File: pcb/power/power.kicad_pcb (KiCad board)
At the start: 2 copper layers, 50 x 40 mm, 233 parts, among them CON1 BARREL_JACK, P1 CONN_01X04, P2 CONN_01X04, P3 CONN_01X04, P4 USB_A, P5 CONN_01X03, P6 CONN_01X03, Q1 MMBT3904, Q2 MMBT3904, Q3 MMBT3904, Q4 MMBT3904, Q5 MMBT3904, Q6 MMBT3904, Q7 DMG2305UX, Q8 DMG2305UX, Q9 DMG2305UX, U1 LM2840, U2 TS30012, U3 TPS2514ADBV, U4 LM324QT

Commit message: Fixed the board. This is rev 2.
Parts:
- removed the REF** at (175.9, 120.0)
- removed the REF** at (160.5, 104.5)
- removed the REF** at (158.0, 101.1)
- removed the REF** at (158.0, 89.3)
- removed the REF** at (149.1, 109.5)
- removed the REF** at (138.0, 113.6)
- removed the REF** at (138.0, 110.3)
- removed the REF** at (166.2, 95.4)
- removed the REF** at (138.0, 111.9)
- removed the REF** at (137.7, 116.7)
- removed the REF** at (145.9, 114.7)
- removed the REF** at (134.6, 98.0)
- removed the REF** at (134.6, 99.3)
- removed the REF** at (134.6, 100.6)
- removed the REF** at (166.9, 90.9)
- removed the REF** at (143.9, 113.9)
- removed the REF** at (165.6, 89.3)
- removed the REF** at (162.1, 86.7)
- removed the REF** at (160.5, 89.3)
- removed the REF** at (159.3, 89.3)
- removed the REF** at (149.9, 95.1)
- added REF**: Via_GND_04, Additional:Via_GND_04, F.Cu at (178.4, 107.2)
- added REF**: Via_GND_04, Additional:Via_GND_04, F.Cu at (173.0, 121.2)
- added REF**: Via_GND_04, Additional:Via_GND_04, F.Cu at (165.1, 108.5)
- added REF**: Via_GND_04, Additional:Via_GND_04, F.Cu at (162.4, 115.7)
- added REF**: Via_GND_04, Additional:Via_GND_04, F.Cu at (158.0, 89.7)
- added REF**: Via_GND_04, Additional:Via_GND_04, F.Cu at (162.3, 110.0)
- added REF**: Via_GND_04, Additional:Via_GND_04, F.Cu at (177.5, 111.8)
- added REF**: Via_GND_04, Additional:Via_GND_04, F.Cu at (141.7, 101.9)
- added REF**: Via_GND_04, Additional:Via_GND_04, F.Cu at (158.0, 100.6)
- added REF**: Via_GND_04, Additional:Via_GND_04, F.Cu at (164.8, 112.5)
- added REF**: Via_GND_04, Additional:Via_GND_04, F.Cu at (160.0, 89.7)
- added REF**: Via_GND_04, Additional:Via_GND_04, F.Cu at (137.4, 93.7)
- added REF**: Via_GND_04, Additional:Via_GND_04, F.Cu at (146.1, 114.8)
- added REF**: Via_GND_04, Additional:Via_GND_04, F.Cu at (147.1, 93.0)
- added REF**: Via_GND_04, Additional:Via_GND_04, F.Cu at (170.9, 121.2)
- added REF**: Via_GND_04, Additional:Via_GND_04, F.Cu at (131.8, 93.7)
- added REF**: Via_GND_04, Additional:Via_GND_04, F.Cu at (144.0, 113.8)
- added REF**: Via_GND_04, Additional:Via_GND_04, F.Cu at (158.0, 102.1)
- added REF**: Via_GND_04, Additional:Via_GND_04, F.Cu at (167.1, 90.7)
- added REF**: Via_GND_04, Additional:Via_GND_04, F.Cu at (154.4, 99.6)
- added REF**: Via_GND_04, Additional:Via_GND_04, F.Cu at (173.7, 111.8)
- added REF**: Via_GND_04, Additional:Via_GND_04, F.Cu at (137.7, 114.0)
- added REF**: Via_GND_04, Additional:Via_GND_04, F.Cu at (158.0, 121.4)
- added REF**: Via_GND_04, Additional:Via_GND_04, F.Cu at (152.0, 99.9)
- added REF**: Via_GND_04, Additional:Via_GND_04, F.Cu at (176.3, 121.2)
- added REF**: Via_GND_04, Additional:Via_GND_04, F.Cu at (148.0, 119.1)
- added REF**: Via_GND_04, Additional:Via_GND_04, F.Cu at (175.0, 111.8)
- added REF**: Via_GND_04, Additional:Via_GND_04, F.Cu at (171.7, 118.1)
- added REF**: Via_GND_04, Additional:Via_GND_04, F.Cu at (175.0, 115.8)
- added REF**: Via_GND_04, Additional:Via_GND_04, F.Cu at (162.6, 95.2)
- added REF**: Via_GND_04, Additional:Via_GND_04, F.Cu at (148.2, 97.9)
- added REF**: Via_GND_04, Additional:Via_GND_04, F.Cu at (137.7, 107.2)
- added REF**: Via_GND_04, Additional:Via_GND_04, F.Cu at (137.7, 105.4)
- added REF**: Via_GND_04, Additional:Via_GND_04, F.Cu at (145.5, 114.0)
- added REF**: Via_GND_04, Additional:Via_GND_04, F.Cu at (155.7, 118.4)
- added REF**: Via_GND_04, Additional:Via_GND_04, F.Cu at (146.8, 109.5)
- added REF**: Via_GND_04, Additional:Via_GND_04, F.Cu at (165.9, 90.7)
- added REF**: Via_GND_04, Additional:Via_GND_04, F.Cu at (134.9, 110.2)
- added REF**: Via_GND_04, Additional:Via_GND_04, F.Cu at (173.5, 118.1)
- added REF**: Via_GND_04, Additional:Via_GND_04, F.Cu at (149.4, 109.5)
- added REF**: Via_GND_04, Additional:Via_GND_04, F.Cu at (134.9, 97.0)
- added REF**: Via_GND_04, Additional:Via_GND_04, F.Cu at (140.7, 97.0)
- added REF**: Via_GND_04, Additional:Via_GND_04, F.Cu at (131.8, 92.5)
- added REF**: Via_GND_04, Additional:Via_GND_04, F.Cu at (161.5, 100.3)
- added REF**: Via_GND_04, Additional:Via_GND_04, F.Cu at (137.4, 92.5)
- added REF**: Via_GND_04, Additional:Via_GND_04, F.Cu at (137.7, 111.5)
- added REF**: Via_GND_04, Additional:Via_GND_04, F.Cu at (178.4, 108.3)
- added REF**: Via_GND_04, Additional:Via_GND_04, F.Cu at (166.4, 104.9)
- added REF**: Via_GND_04, Additional:Via_GND_04, F.Cu at (149.5, 118.4)
- added REF**: Via_GND_04, Additional:Via_GND_04, F.Cu at (158.8, 115.1)
- added REF**: Via_GND_04, Additional:Via_GND_04, F.Cu at (160.0, 102.1)
- added REF**: Via_GND_04, Additional:Via_GND_04, F.Cu at (175.0, 113.8)
- added REF**: Via_GND_04, Additional:Via_GND_04, F.Cu at (161.0, 121.4)
- added REF**: Via_GND_04, Additional:Via_GND_04, F.Cu at (158.0, 122.7)
- added REF**: Via_GND_04, Additional:Via_GND_04, F.Cu at (175.0, 118.1)
- added REF**: Via_GND_04, Additional:Via_GND_04, F.Cu at (145.5, 90.2)
- added REF**: Via_GND_04, Additional:Via_GND_04, F.Cu at (137.7, 112.8)
- added REF**: Via_GND_04, Additional:Via_GND_04, F.Cu at (166.4, 119.4)
- added REF**: Via_GND_04, Additional:Via_GND_04, F.Cu at (142.2, 97.0)
- added REF**: Via_GND_04, Additional:Via_GND_04, F.Cu at (138.9, 99.6)
- Q1, Q2, Q3, Q4, Q5, Q6, Q7, Q8, Q9: footprint TO_SOT_Packages_SMD:SOT-23_Handsoldering -> TO_SOT_Packages_SMD:SOT-23
- moved REF** 42.4 mm to (136.7, 97.0)
- moved REF** 42.2 mm to (136.7, 99.6)
- moved REF** 28.7 mm to (134.9, 98.3)
- moved REF** 28.7 mm to (153.7, 89.7)
- moved REF** 28.0 mm to (134.9, 99.6)
- moved REF** 27.5 mm to (137.7, 110.2)
- moved REF** 27.1 mm to (136.7, 100.8)
- moved REF** 27.1 mm to (155.2, 89.7)
- moved REF** 26.8 mm to (134.9, 100.8)
- moved REF** 25.0 mm to (136.7, 98.3)
- moved REF** 20.0 mm to (176.0, 107.2)
- moved REF** 18.4 mm to (158.8, 116.6)
- moved REF** 18.0 mm to (161.0, 105.2)
- moved REF** 14.9 mm to (178.3, 116.3)
- moved REF** 14.5 mm to (160.0, 104.1)
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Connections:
- C11 pad 1: PWM_OLED -> Net-(C11-Pad1)
- Q1 pad 2: Net-(D6-Pad1) -> LED_GND
- Q1 pad 3: LED_GND -> Net-(D6-Pad1)
- Q2 pad 2: Net-(D7-Pad1) -> LED_GND
- Q2 pad 3: LED_GND -> Net-(D7-Pad1)
- Q3 pad 2: Net-(D8-Pad1) -> LED_GND
- Q3 pad 3: LED_GND -> Net-(D8-Pad1)
- Q4 pad 2: V20 -> Net-(D6-Pad2)
- Q4 pad 3: Net-(D6-Pad2) -> V20
- Q5 pad 2: V20 -> Net-(D7-Pad2)
- Q5 pad 3: Net-(D7-Pad2) -> V20
- Q6 pad 2: V20 -> Net-(D8-Pad2)
- Q6 pad 3: Net-(D8-Pad2) -> V20
- Q7 pad 1: V20 -> Net-(D6-Pad2)
- Q7 pad 2: Net-(D6-Pad2) -> V20
- Q8 pad 1: V20 -> Net-(D7-Pad2)
- Q8 pad 2: Net-(D7-Pad2) -> V20
- Q9 pad 1: V20 -> Net-(D8-Pad2)
- Q9 pad 2: Net-(D8-Pad2) -> V20
- R18 pad 1: Net-(C9-Pad1) -> PWM_OLED
- R18 pad 2: Net-(R18-Pad2) -> Net-(C11-Pad1)
- R20 pad 1: PWM_OLED -> Net-(C11-Pad1)
- U4 pad 12: Net-(R18-Pad2) -> Net-(C9-Pad1)
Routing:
- net Net-(C12-Pad1): track 22.3 -> 3.37 mm
- net Net-(C4-Pad2): track 25.1 -> 17.2 mm
- net LED_R: track 83.2 -> 89.1 mm, vias 6 -> 5
- net V20: track 178.9 -> 174.4 mm
- net Net-(R18-Pad2): track 4.44 -> 0.00 mm
- net Net-(C11-Pad1): track 0.00 -> 4.42 mm, vias 0 -> 2
- net Net-(C9-Pad1): track 5.36 -> 9.69 mm
- net Net-(C13-Pad1): track 9.96 -> 5.96 mm
- net Net-(C2-Pad1): track 7.30 -> 3.54 mm
- net Net-(D8-Pad1): track 16.4 -> 13.3 mm
- net Net-(C4-Pad1): track 4.50 -> 1.54 mm
- net Net-(D7-Pad1): track 12.9 -> 10.0 mm
- net Net-(D6-Pad1): track 7.81 -> 10.6 mm, vias 2 -> 1
- net V28: track 28.7 -> 31.5 mm
- net PWM_OLED: track 51.8 -> 49.1 mm, vias 3 -> 1
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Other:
- net class Default: clearance 0.2 -> 0.19
- rule trace_clearance: 0.2 -> 0.19
- board text removed: "C22"
- board text removed: "D10"
- board text removed: "D11"
- board text removed: "D2"
- board text removed: "D4"
- board text removed: "D6"
- board text removed: "D7"
- board text removed: "D8"
- board text removed: "D9"
- board text removed: "U3"

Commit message: Some minor changes. Rev2 ready now.
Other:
- board text added: "Max & Elmar February 2017"
- board text added: "Swakeup Power Rev2"
- board text removed: "Max & Elmar December 2016"
- board text removed: "Swakeup Power Rev1"
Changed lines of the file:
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@@
   (layers
     (0 F.Cu signal)
-    (31 B.Cu signal)
+    (31 B.Cu signal hide)
     (32 B.Adhes user hide)
-    (33 F.Adhes user hide)
+    (33 F.Adhes user)
     (34 B.Paste user hide)
     (35 F.Paste user hide)
     (36 B.SilkS user hide)
-    (37 F.SilkS user)
+    (37 F.SilkS user hide)
     (38 B.Mask user hide)
     (39 F.Mask user hide)
@@
   )
   (setup
-    (last_trace_width 0.25)
+    (last_trace_width 0.75)
     (user_trace_width 0.5)
     (user_trace_width 0.75)
@@
     (tags SOT-23)
     (attr smd)
-    (fp_text reference Q9 (at -1.778 -1.651 360) (layer F.SilkS)
+    (fp_text reference Q9 (at 0 2.54 360) (layer F.SilkS)
       (effects (font (size 1 1) (thickness 0.15)))
     )
@@
     (tags SOT-23)
     (attr smd)
-    (fp_text reference Q7 (at -2.413 0 360) (layer F.SilkS)
+    (fp_text reference Q7 (at 0 2.667 360) (layer F.SilkS)
       (effects (font (size 1 1) (thickness 0.15)))
     )
@@
     (tags SOT-23)
     (attr smd)
-    (fp_text reference Q6 (at -1.397 -2.032 180) (layer F.SilkS)
+    (fp_text reference Q6 (at 0 2.667 180) (layer F.SilkS)
       (effects (font (size 1 1) (thickness 0.15)))
     )
@@
     (tags SOT-23)
     (attr smd)
-    (fp_text reference Q5 (at 0 2.54 360) (layer F.SilkS)
+    (fp_text reference Q5 (at 0 -2.54 360) (layer F.SilkS)
       (effects (font (size 1 1) (thickness 0.15)))
     )
@@
     (tags SOT-23)
     (attr smd)
-    (fp_text reference Q4 (at 0 -4.191 180) (layer F.SilkS)
+    (fp_text reference Q4 (at 0 2.54 180) (layer F.SilkS)
       (effects (font (size 1 1) (thickness 0.15)))
     )
@@
   (module Additional:Bourns_SRN3015 (layer F.Cu)
     (at 174.4726 102.616 90)
-    (fp_text reference L3 (at -2.286 -2.5146 180) (layer F.SilkS)
+    (fp_text reference L3 (at -2.413 -2.5146 180) (layer F.SilkS)
       (effects (font (size 1 1) (thickness 0.15)))
     )
@@
     (tags "capacitor 0603")
     (attr smd)
-    (fp_text reference R26 (at -2.413 0.127 270) (layer F.SilkS)
+    (fp_text reference R26 (at -2.413 0 270) (layer F.SilkS)
       (effects (font (size 0.5 0.5) (thickness 0.125)))
     )
@@
     (tags "capacitor 0603")
     (attr smd)
-    (fp_text reference R24 (at 0.1778 -1.524 360) (layer F.SilkS)
+    (fp_text reference R24 (at 0.127 1.524 360) (layer F.SilkS)
       (effects (font (size 0.5 0.5) (thickness 0.125)))
     )
@@
     (tags "capacitor 0603")
     (attr smd)
-    (fp_text reference C5 (at 2.2606 0.0508 360) (layer F.SilkS)
+    (fp_text reference C5 (at 0.4572 1.2446 360) (layer F.SilkS)
       (effects (font (size 0.5 0.5) (thickness 0.125)))
     )
@@
     (tags SOT-23)
     (attr smd)
-    (fp_text reference Q8 (at 3.556 0.254 360) (layer F.SilkS)
+    (fp_text reference Q8 (at 2.794 0 360) (layer F.SilkS)
       (effects (font (size 1 1) (thickness 0.15)))
     )
@@
     (arrow2b (pts (xy 172.4906 129.817) (xy 171.364096 130.403421)))
   )
-  (gr_text "Swakeup\nPower \nRev1" (at 142.494 111.76) (layer B.SilkS)
+  (gr_text "Swakeup\nPower \nRev2" (at 142.494 111.76) (layer B.SilkS)
     (effects (font (size 1 1) (thickness 0.2)) (justify left mirror))
   )
-  (gr_text "Max & Elmar \nDecember 2016\n" (at 142.748 116.586) (layer B.SilkS)
+  (gr_text "Max & Elmar \nFebruary 2017\n" (at 142.748 116.586) (layer B.SilkS)
     (effects (font (size 1 1) (thickness 0.2)) (justify left mirror))
   )
@@
   (segment (start 151.7516 105.065598) (end 151.765 105.052198) (width 0.25) (layer F.Cu) (net 5))
   (segment (start 153.9766 103.1882) (end 154.0644 103.1882) (width 0.25) (layer F.Cu) (net 5) (status 30))
+  (segment (start 177.5206 109.7178) (end 176.8578 109.7178) (width 0.75) (layer F.Cu) (net 6))
+  (segment (start 176.8578 109.7178) (end 176.106 108.966) (width 0.75) (layer F.Cu) (net 6))
   (segment (start 177.5206 109.7178) (end 177.5206 106.9086) (width 0.25) (layer F.Cu) (net 6))
   (segment (start 168.148 107.6452) (end 169.291 106.5022) (width 0.25) (layer F.Cu) (net 6))
@@
   (segment (start 177.5206 106.9086) (end 177.1142 106.5022) (width 0.25) (layer F.Cu) (net 6))
   (segment (start 177.58 122.5) (end 177.58 118.398) (width 0.5) (layer F.Cu) (net 6))
-  (segment (start 176.106 116.924) (end 176.106 108.966) (width 0.5) (layer F.Cu) (net 6))
   (segment (start 177.58 118.398) (end 176.106 116.924) (width 0.5) (layer F.Cu) (net 6))
-  (segment (start 177.5206 109.7178) (end 176.8578 109.7178) (width 0.5) (layer F.Cu) (net 6))
-  (segment (start 176.8578 109.7178) (end 176.106 108.966) (width 0.5) (layer F.Cu) (net 6))
+  (segment (start 176.106 116.924) (end 176.106 108.966) (width 0.5) (layer F.Cu) (net 6))
   (segment (start 177.5206 109.7178) (end 178.6153 109.7178) (width 0.5) (layer F.Cu) (net 6))
   (segment (start 178.6153 109.7178) (end 178.816 109.9185) (width 0.5) (layer F.Cu) (net 6))

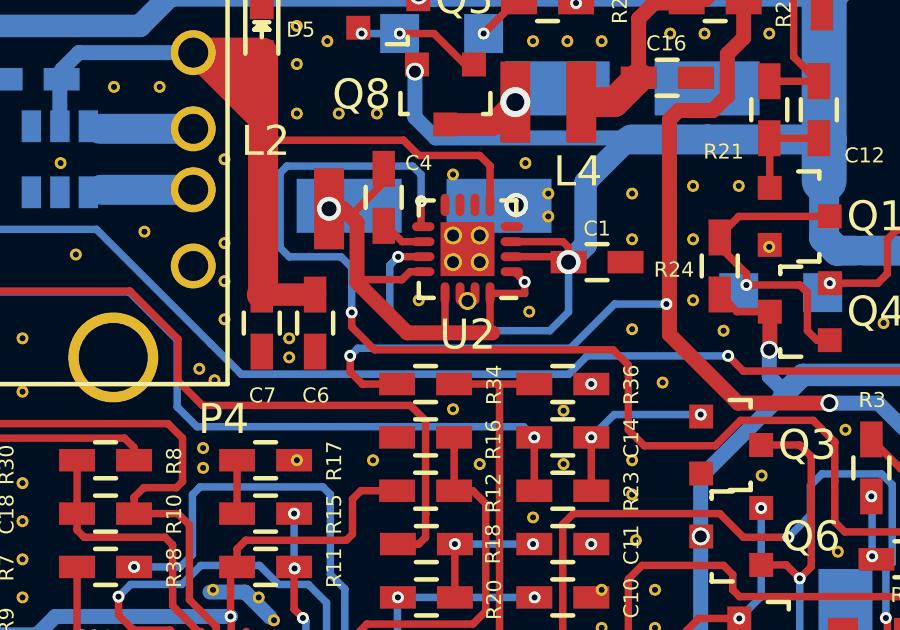
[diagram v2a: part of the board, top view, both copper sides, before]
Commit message: Produced some output. Soldermask changed: Less clearance.
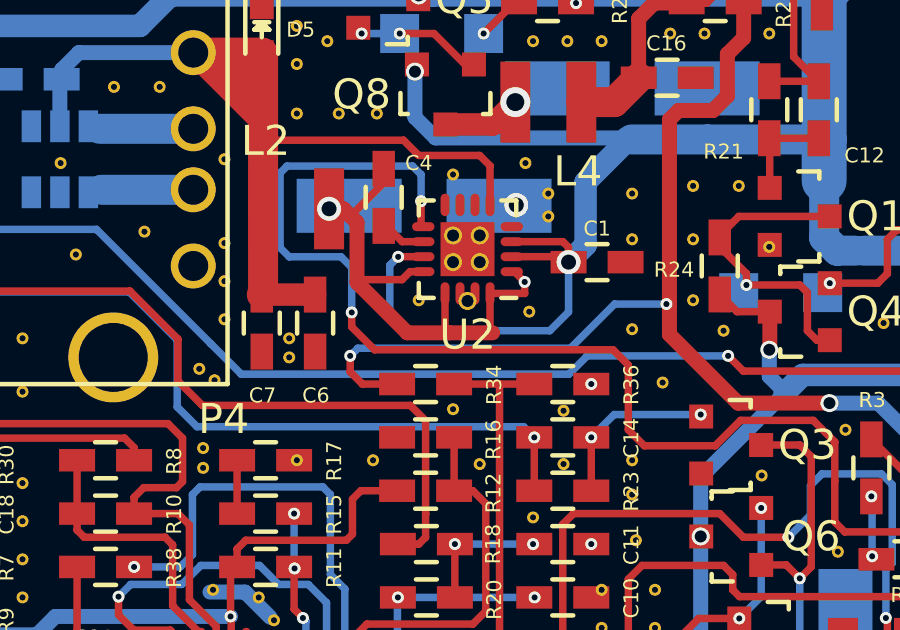
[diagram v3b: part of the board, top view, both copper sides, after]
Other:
- rule pad_to_mask_clearance: 0 -> 0.05
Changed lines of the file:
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@@
   (general
     (links 365)
-    (no_connects 1)
-    (area 129.899999 84.899999 180.100001 125.100001)
+    (no_connects 0)
+    (area 118.064287 79.5 200.254 136.700001)
     (thickness 1.6)
     (drawings 20)
-    (tracks 978)
+    (tracks 980)
     (zones 0)
     (modules 272)
@@
   (layers
     (0 F.Cu signal)
-    (31 B.Cu signal hide)
+    (31 B.Cu signal)
     (32 B.Adhes user hide)
-    (33 F.Adhes user)
+    (33 F.Adhes user hide)
     (34 B.Paste user hide)
     (35 F.Paste user hide)
@@
   )
   (setup
-    (last_trace_width 0.75)
+    (last_trace_width 0.25)
     (user_trace_width 0.5)
     (user_trace_width 0.75)
@@
     (pad_size 0.9 0.9)
     (pad_drill 0)
-    (pad_to_mask_clearance 0)
+    (pad_to_mask_clearance 0.05)
     (aux_axis_origin 0 0)
     (visible_elements FFFEFF7F)
@@
       (drillshape 0)
       (scaleselection 1)
-      (outputdirectory output/))
+      (outputdirectory output/rev2/))
   )
   (net 0 "")
@@
   (segment (start 150.3212 102.1882) (end 149.794 101.661) (width 0.25) (layer F.Cu) (net 4))
   (segment (start 149.794 101.661) (end 149.7076 101.661) (width 0.25) (layer F.Cu) (net 4))
+  (segment (start 151.7516 103.9132) (end 151.7516 105.225998) (width 0.25) (layer F.Cu) (net 5))
+  (segment (start 151.892 105.156) (end 151.892 105.225998) (width 0.25) (layer F.Cu) (net 5))
+  (segment (start 151.821598 105.156) (end 151.892 105.156) (width 0.25) (layer F.Cu) (net 5))
+  (segment (start 151.7516 105.225998) (end 151.821598 105.156) (width 0.25) (layer F.Cu) (net 5))
   (segment (start 149.7076 99.761) (end 149.7076 100.2284) (width 0.25) (layer F.Cu) (net 5))
   (segment (start 149.7076 100.2284) (end 148.6027 101.3333) (width 0.25) (layer F.Cu) (net 5))
@@
   (segment (start 148.3614 101.092) (end 148.6027 101.3333) (width 0.5) (layer F.Cu) (net 5))
   (segment (start 148.6027 101.3333) (end 148.8186 101.5492) (width 0.5) (layer F.Cu) (net 5))
-  (segment (start 150.495 105.225998) (end 153.3398 105.225998) (width 0.5) (layer F.Cu) (net 5))
+  (segment (start 150.495 105.225998) (end 151.892 105.225998) (width 0.5) (layer F.Cu) (net 5))
+  (segment (start 151.892 105.225998) (end 153.3398 105.225998) (width 0.5) (layer F.Cu) (net 5))
   (segment (start 148.8186 103.549598) (end 150.495 105.225998) (width 0.5) (layer F.Cu) (net 5))
   (segment (start 148.8186 101.5492) (end 148.8186 103.549598) (width 0.5) (layer F.Cu) (net 5))
@@
   (segment (start 153.2636 105.053598) (end 153.2636 105.065598) (width 0.25) (layer F.Cu) (net 5))
   (segment (start 153.2516 105.065598) (end 153.2636 105.053598) (width 0.25) (layer F.Cu) (net 5))
-  (segment (start 151.7516 103.9132) (end 151.7516 105.065598) (width 0.25) (layer F.Cu) (net 5) (status 10))
-  (segment (start 151.765 105.052198) (end 151.765 105.065598) (width 0.25) (layer F.Cu) (net 5))
-  (segment (start 151.7516 105.065598) (end 151.765 105.052198) (width 0.25) (layer F.Cu) (net 5))
   (segment (start 153.9766 103.1882) (end 154.0644 103.1882) (width 0.25) (layer F.Cu) (net 5) (status 30))
   (segment (start 177.5206 109.7178) (end 176.8578 109.7178) (width 0.75) (layer F.Cu) (net 6))
